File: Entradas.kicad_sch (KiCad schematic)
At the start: 14 parts, among them IC1 MCP6486T-E_OT, J10 Terminal_Sensores_Nivel, J11 Terminal_Sensor_Flujo, J4 Terminal_Sensor_pH, J5 Terminal_Sensor_Temp_Sumerg, J6 Terminal_Sensor_TDS, J7 Terminal_Sensor_Temp_Sumerg, J8 Terminal_Sensor_Iluminacion, J9 Terminal_Sensor_Temp_y_Hum

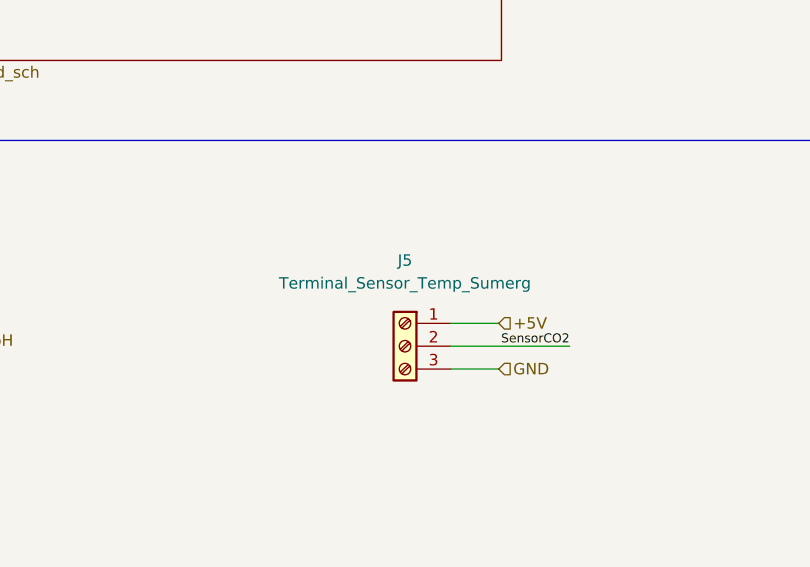
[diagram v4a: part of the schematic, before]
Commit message: Cambios en SCH y PCB.
Se cambio el adaptador de nivel 5-3,3V por un circuito con MOSFET 2N7002, dado que ya no hay stock del NXB. Se modificó el footprint del expansor I/O por uno thorugh-hole.
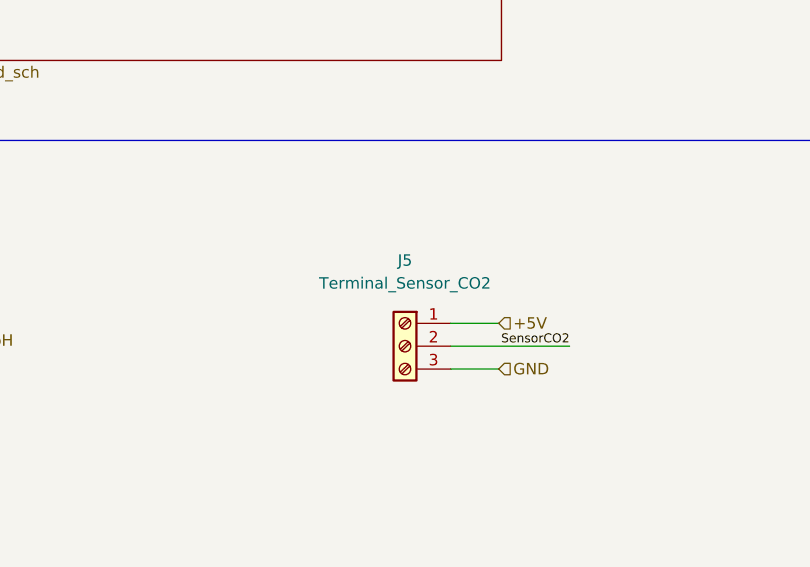
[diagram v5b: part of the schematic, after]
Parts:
- J5: value Terminal_Sensor_Temp_Sumerg -> Terminal_Sensor_CO2
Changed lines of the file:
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@@
     (in_bom yes) (on_board yes)
     (property "Reference" "J5" (id 0) (at 118.1862 95.885 0))
-    (property "Value" "Terminal_Sensor_Temp_Sumerg" (id 1) (at 118.1862 98.425 0))
+    (property "Value" "Terminal_Sensor_CO2" (id 1) (at 118.1862 98.425 0))
     (property "Footprint" "TB002-500-03BE:SHDR3W100P0X500_1X3_1500X760X1000P" (id 2) (at 118.1862 105.41 0)
       (effects (font (size 1.27 1.27)) hide)

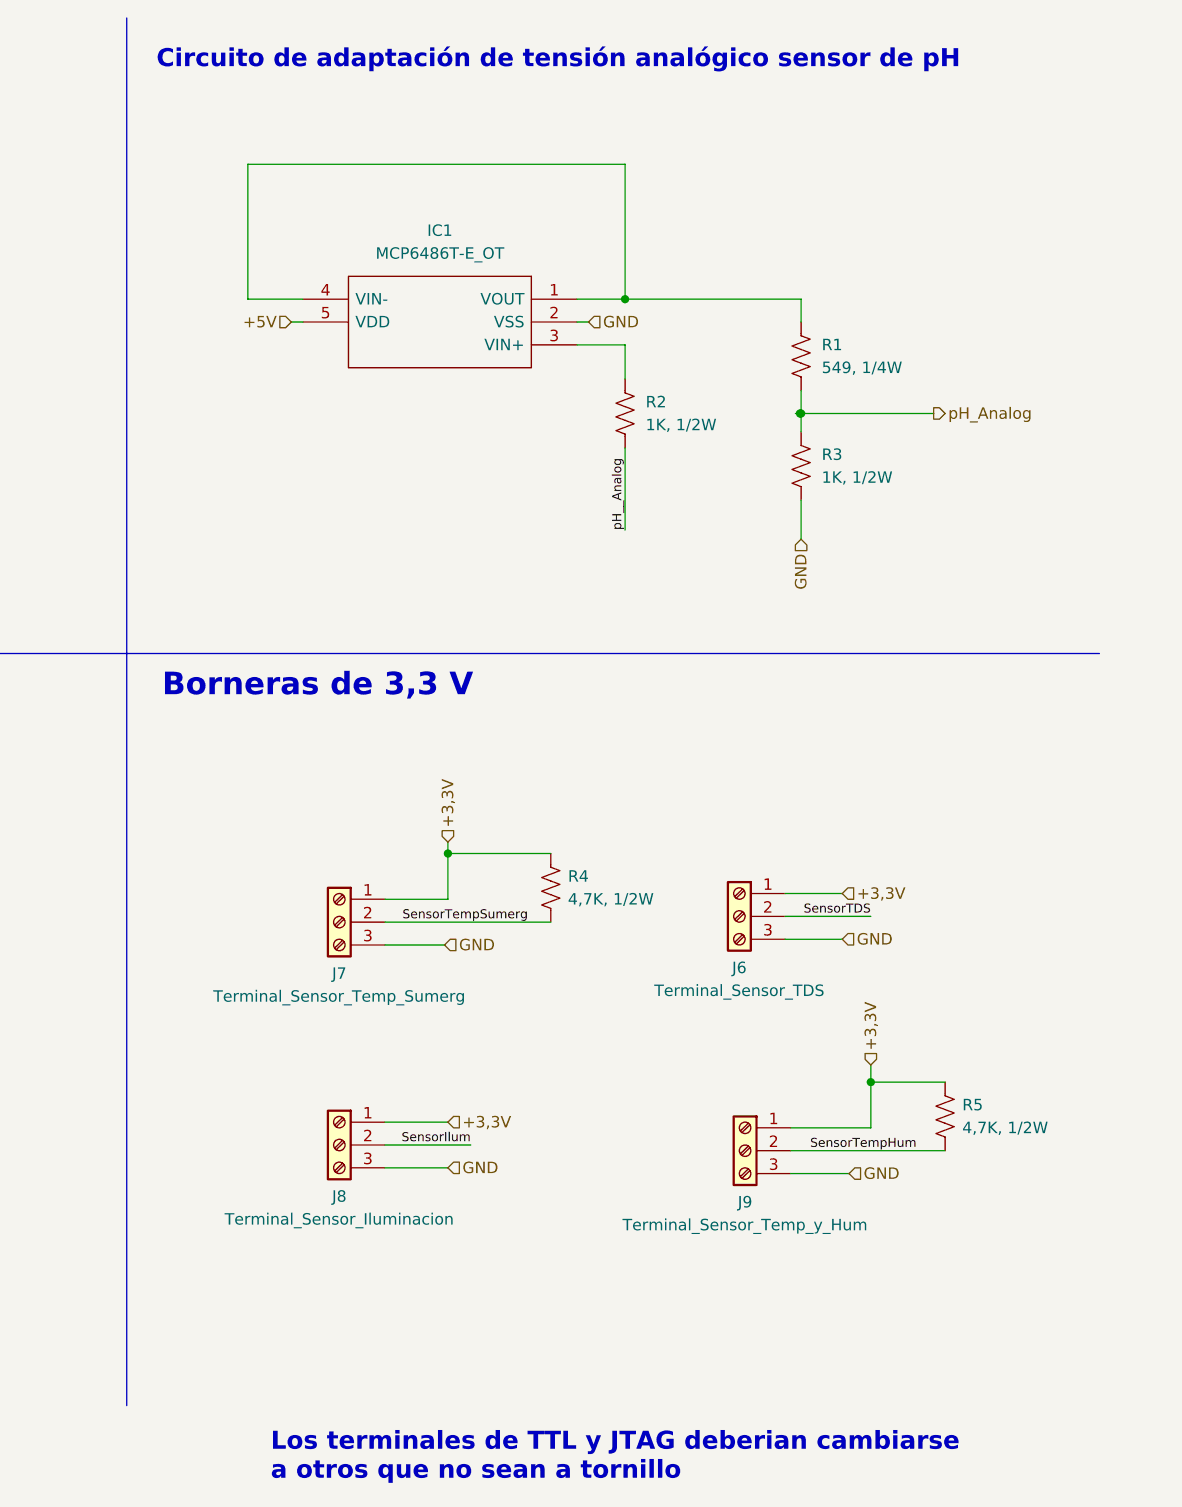
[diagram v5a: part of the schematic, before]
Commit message: Se finalizó con el PCB del prototipo.
Dado que se buscó a toda costa que el PCB fuera de 1 capa, en varios puntos del circuito se tuvieron que agregar pin headers individuales para conectar a 3V3 y GND, junto con tiras de pin headers. Cada una de estas se conectara luego entre si mediante cables.

Tambien se generaron los archivos Gerber y BOM.
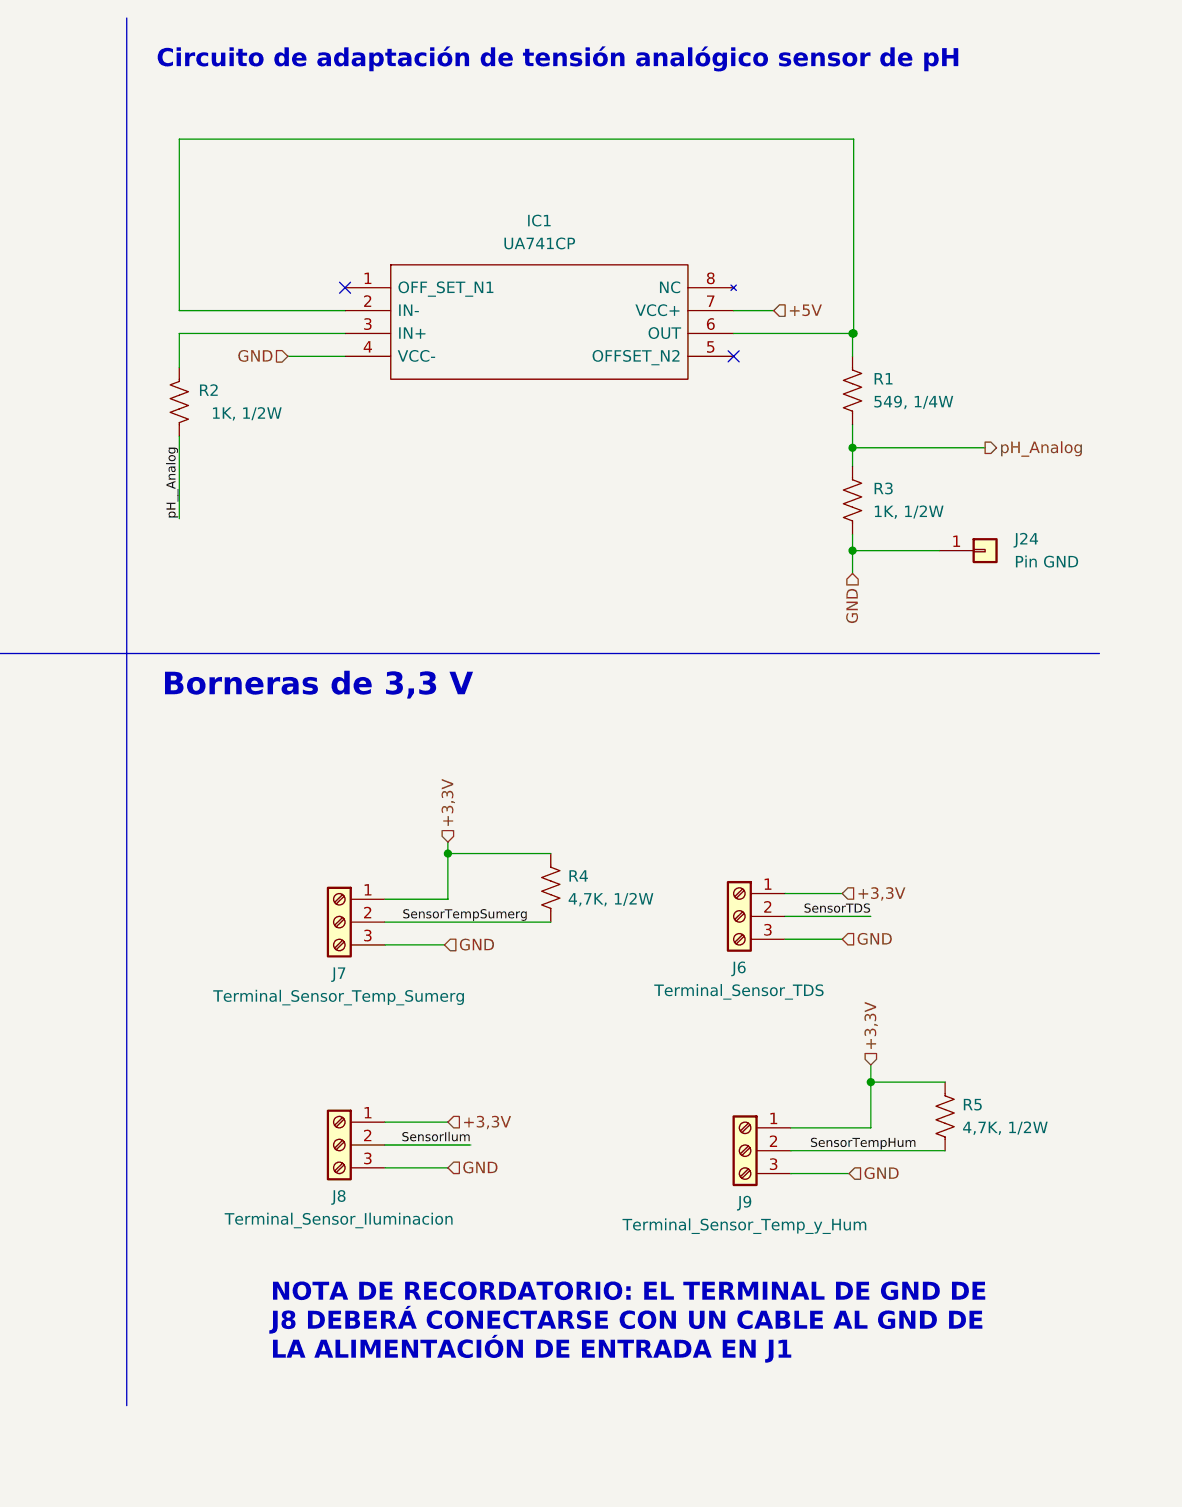
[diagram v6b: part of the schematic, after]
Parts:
- removed IC1: MCP6486T-E_OT, MCP6486T-E_OT:MCP6486RT-E&slash_OT, symbol MCP6486T-E/OT:MCP6486T-E_OT
- added IC1: UA741CP, UA741CP:DIP794W53P254L959H508Q8N, symbol UA741CP:UA741CP
- added J24: Pin GND, Connector_PinHeader_2.54mm:PinHeader_1x01_P2.54mm_Vertical, symbol Connector_Generic:Conn_01x01
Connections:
- net +5V: now also IC1.7 (VCC+)
- net GND: now also IC1.4 (VCC-), J24.1 (Pin_1)
- net at R1.1: now also IC1.2 (IN-), IC1.6 (OUT)
- net at R2.1: now also IC1.3 (IN+)
- no-connect marks 0 -> 2
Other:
- note added: "NOTA DE RECORDATORIO: EL TERMINAL DE GND DE J8 DEBERÁ CONECTARSE CON UN CABLE AL GND DE LA ALIMENTACIÓN DE ENTRADA EN J1"
- note removed: "Los terminales de TTL y JTAG deberian cambiarse a otros que no sean a tornillo"
- moved on the sheet: R1, R2, R3

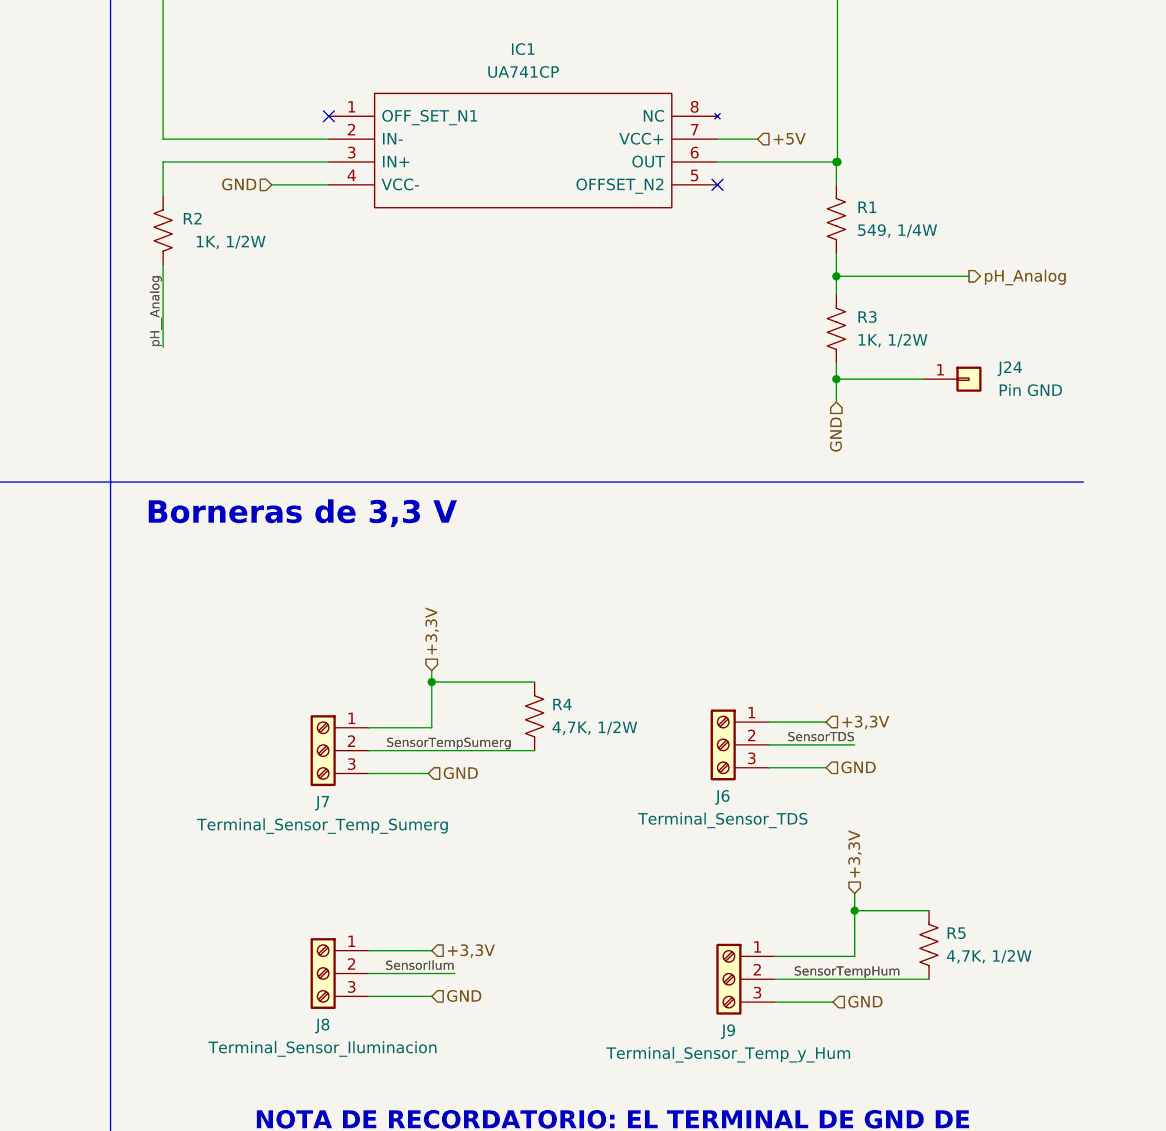
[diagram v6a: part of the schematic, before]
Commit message: Se modificaron algunos componentes, según disponibilidad
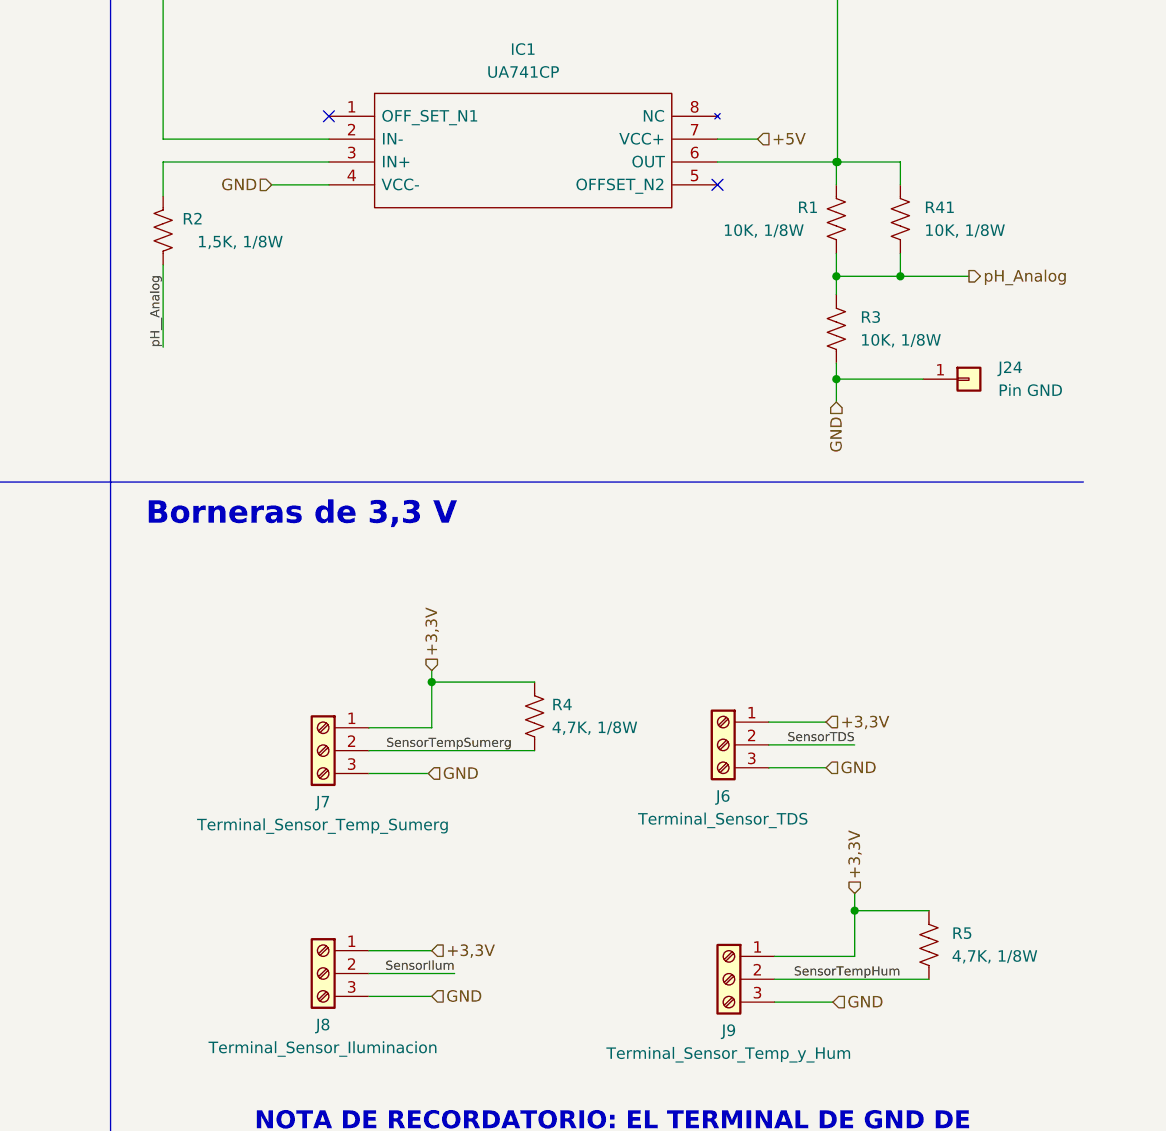
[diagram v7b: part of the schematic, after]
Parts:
- added R41: 10K, 1/8W, Resistor_SMD:R_0805_2012Metric, symbol Device:R_US
- R1: value 549, 1/4W -> 10K, 1/8W
- R2: value 1K, 1/2W -> 1,5K, 1/8W
- R3: value 1K, 1/2W -> 10K, 1/8W
- R4, R5: value 4,7K, 1/2W -> 4,7K, 1/8W
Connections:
- net pH_Analog: now also R41.2
- net at IC1.2 (IN-), IC1.6 (OUT), R1.1: now also R41.1
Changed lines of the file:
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@@
   (junction (at 257.683 59.69) (diameter 0) (color 0 0 0 0)
+  )
+  (junction (at 264.795 59.69) (diameter 0) (color 0 0 0 0)
   )
   (junction (at 259.715 130.175) (diameter 0) (color 0 0 0 0)
@@
     (stroke (width 0) (type default) (color 0 0 0 0))
   )
+  (wire (pts (xy 264.795 59.69) (xy 272.415 59.69))
+    (stroke (width 0) (type default) (color 0 0 0 0))
+  )
   (wire (pts (xy 60.325 155.575) (xy 71.755 155.575))
     (stroke (width 0) (type default) (color 0 0 0 0))
   )
-  (wire (pts (xy 257.683 59.69) (xy 272.415 59.69))
+  (wire (pts (xy 257.683 59.69) (xy 264.795 59.69))
     (stroke (width 0) (type default) (color 0 0 0 0))
   )
@@
     (stroke (width 0) (type default) (color 0 0 0 0))
   )
+  (wire (pts (xy 264.795 49.53) (xy 264.795 46.99))
+    (stroke (width 0) (type default) (color 0 0 0 0))
+  )
   (wire (pts (xy 205.74 112.395) (xy 224.155 112.395))
     (stroke (width 0) (type default) (color 0 0 0 0))
@@
     (stroke (width 0) (type default) (color 0 0 0 0))
   )
+  (wire (pts (xy 264.795 46.99) (xy 257.81 46.99))
+    (stroke (width 0) (type default) (color 0 0 0 0))
+  )
   (wire (pts (xy 182.88 25.4) (xy 257.81 25.4))
     (stroke (width 0) (type default) (color 0 0 0 0))
@@
   )
   (wire (pts (xy 128.905 36.83) (xy 133.477 36.83))
+    (stroke (width 0) (type default) (color 0 0 0 0))
+  )
+  (wire (pts (xy 264.795 57.15) (xy 264.795 59.69))
     (stroke (width 0) (type default) (color 0 0 0 0))
   )
@@
     (pin "2")
     (pin "3")
+  )
+  (symbol (lib_id "Device:R_US") (at 264.795 53.34 0) (unit 1)
+    (in_bom yes) (on_board yes) (fields_autoplaced)
+    (property "Reference" "R41" (id 0) (at 267.462 52.0699 0)
+      (effects (font (size 1.27 1.27)) (justify left))
+    )
+    (property "Value" "10K, 1/8W" (id 1) (at 267.462 54.6099 0)
+      (effects (font (size 1.27 1.27)) (justify left))
+    )
+    (property "Footprint" "Resistor_SMD:R_0805_2012Metric" (id 2) (at 265.811 53.594 90)
+      (effects (font (size 1.27 1.27)) hide)
+    )
+    (property "Datasheet" "~" (id 3) (at 264.795 53.34 0)
+      (effects (font (size 1.27 1.27)) hide)
+    )
+    (pin "1")
+    (pin "2")
   )
   (symbol (lib_id "Connector:Screw_Terminal_01x03") (at 245.745 137.795 0) (mirror y) (unit 1)
@@
       (effects (font (size 1.27 1.27)) (justify left))
     )
-    (property "Value" "4,7K, 1/2W" (id 1) (at 226.06 109.8549 0)
+    (property "Value" "4,7K, 1/8W" (id 1) (at 226.06 109.8549 0)
       (effects (font (size 1.27 1.27)) (justify left))
     )
@@
   )
   (symbol (lib_id "Device:R_US") (at 257.683 53.34 0) (unit 1)
-    (in_bom yes) (on_board yes) (fields_autoplaced)
-    (property "Reference" "R1" (id 0) (at 259.969 52.0699 0)
-      (effects (font (size 1.27 1.27)) (justify left))
-    )
-    (property "Value" "549, 1/4W" (id 1) (at 259.969 54.6099 0)
+    (in_bom yes) (on_board yes)
+    (property "Reference" "R1" (id 0) (at 253.365 52.07 0)
+      (effects (font (size 1.27 1.27)) (justify left))
+    )
+    (property "Value" "10K, 1/8W" (id 1) (at 245.11 54.61 0)
       (effects (font (size 1.27 1.27)) (justify left))
     )
@@
   (symbol (lib_id "Device:R_US") (at 267.97 133.985 0) (unit 1)
     (in_bom yes) (on_board yes) (fields_autoplaced)
-    (property "Reference" "R5" (id 0) (at 269.875 132.7149 0)
-      (effects (font (size 1.27 1.27)) (justify left))
-    )
-    (property "Value" "4,7K, 1/2W" (id 1) (at 269.875 135.2549 0)
+    (property "Reference" "R5" (id 0) (at 270.51 132.7149 0)
+      (effects (font (size 1.27 1.27)) (justify left))
+    )
+    (property "Value" "4,7K, 1/8W" (id 1) (at 270.51 135.2549 0)
       (effects (font (size 1.27 1.27)) (justify left))
     )
@@
   (symbol (lib_id "Device:R_US") (at 257.683 65.532 0) (unit 1)
     (in_bom yes) (on_board yes) (fields_autoplaced)
-    (property "Reference" "R3" (id 0) (at 259.969 64.2619 0)
-      (effects (font (size 1.27 1.27)) (justify left))
-    )
-    (property "Value" "1K, 1/2W" (id 1) (at 259.969 66.8019 0)
+    (property "Reference" "R3" (id 0) (at 260.35 64.2619 0)
+      (effects (font (size 1.27 1.27)) (justify left))
+    )
+    (property "Value" "10K, 1/8W" (id 1) (at 260.35 66.8019 0)
       (effects (font (size 1.27 1.27)) (justify left))
     )
@@
       (effects (font (size 1.27 1.27)) (justify left))
     )
-    (property "Value" "1K, 1/2W" (id 1) (at 194.31 55.88 0)
-      (effects (font (size 1.27 1.27)) (justify left))
-    )
+    (property "Value" "1,5K, 1/8W" (id 1) (at 196.215 55.88 0)
+      (effects (font (size 1.27 1.27)) (justify left))
+    )
